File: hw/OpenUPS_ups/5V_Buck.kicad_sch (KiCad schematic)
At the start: 44 parts, among them U301 TPS51397A

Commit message: More cleanups and stuff
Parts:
- removed C?: 100n 50V, Capacitor_SMD:C_0603_1608Metric, symbol Device:C_Small
- removed C? (x2): 865080243008, Capacitor_SMD:CP_Elec_6.3x5.7, symbol Device:C_Polarized
- removed C?: 1u, Capacitor_SMD:C_0603_1608Metric, symbol Device:C_Small
- removed C?: 56p, Capacitor_SMD:C_0603_1608Metric, symbol Device:C_Small
- removed C?: 10u 35V, Capacitor_SMD:C_1206_3216Metric, symbol Device:C
- removed C? (x2): 47u 35V, Capacitor_SMD:CP_Elec_6.3x7.7, symbol Device:C_Polarized
- removed C?: ?, Capacitor_SMD:C_0603_1608Metric, symbol Device:C_Small
- removed C?: 1u 35V, Capacitor_SMD:C_1206_3216Metric, symbol Device:C
- removed C?: 12n, Capacitor_SMD:C_0603_1608Metric, symbol Device:C_Small
- removed L?: SRP1038C-3R3M, Inductor_SMD:L_Bourns_SRP1038C_10.0x10.0mm, symbol Device:L
- removed Q? (x2): Q_NMOS_GDS, Package_TO_SOT_SMD:TO-263-2, symbol Device:Q_NMOS_GDS
- removed R?: 4k7, Resistor_SMD:R_0603_1608Metric, symbol Device:R_Small
- removed R? (x4): ?, Resistor_SMD:R_0603_1608Metric, symbol Device:R_Small
- removed R?: 100k, Resistor_SMD:R_0603_1608Metric, symbol Device:R_Small
- removed R?: 0R, Resistor_SMD:R_0603_1608Metric, symbol Device:R_Small
- removed R?: 1k, Resistor_SMD:R_0603_1608Metric, symbol Device:R_Small
- removed U?: NCP3011, Package_SO:TSSOP-16_4.4x5mm_P0.65mm, symbol open-psu:NCP3011
- gave numbers to parts that had none: 2
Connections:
- net EN: now reaches R306.1, R307.2, U301.12 (EN)
- no-connect marks 2 -> 0
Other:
- note removed: "ISen"
- moved on the sheet: C301, C302, C303, C304, C305, C306, C307, C308, C309, C310, L301, R301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

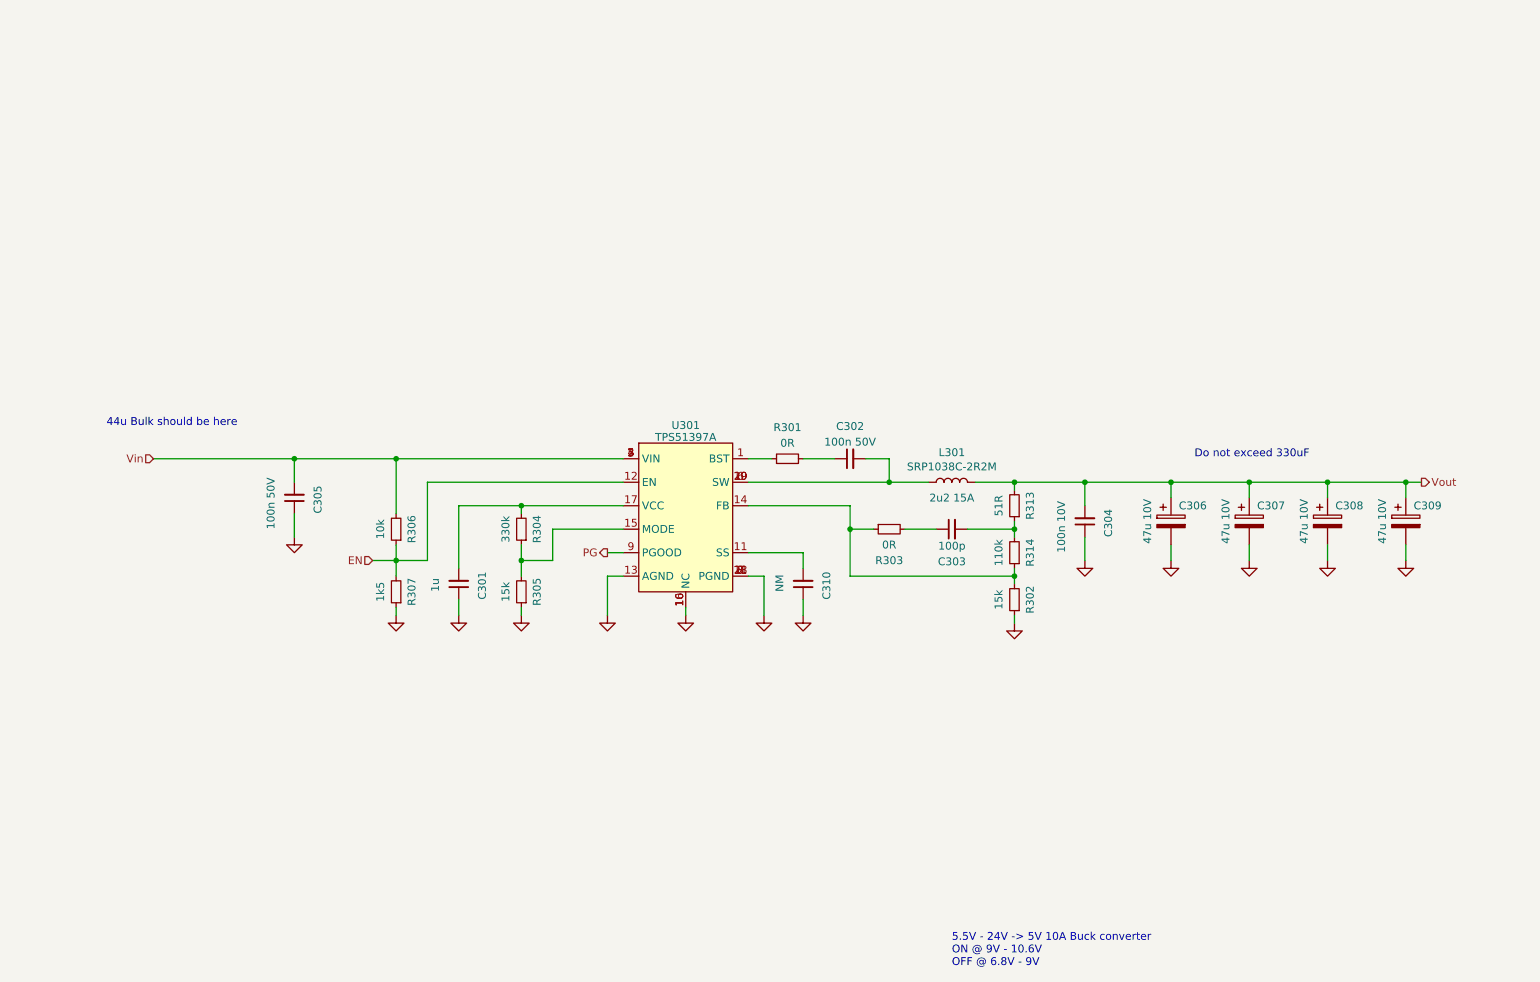
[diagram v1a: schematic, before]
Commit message: Work on 5V; EN pins taken care of.
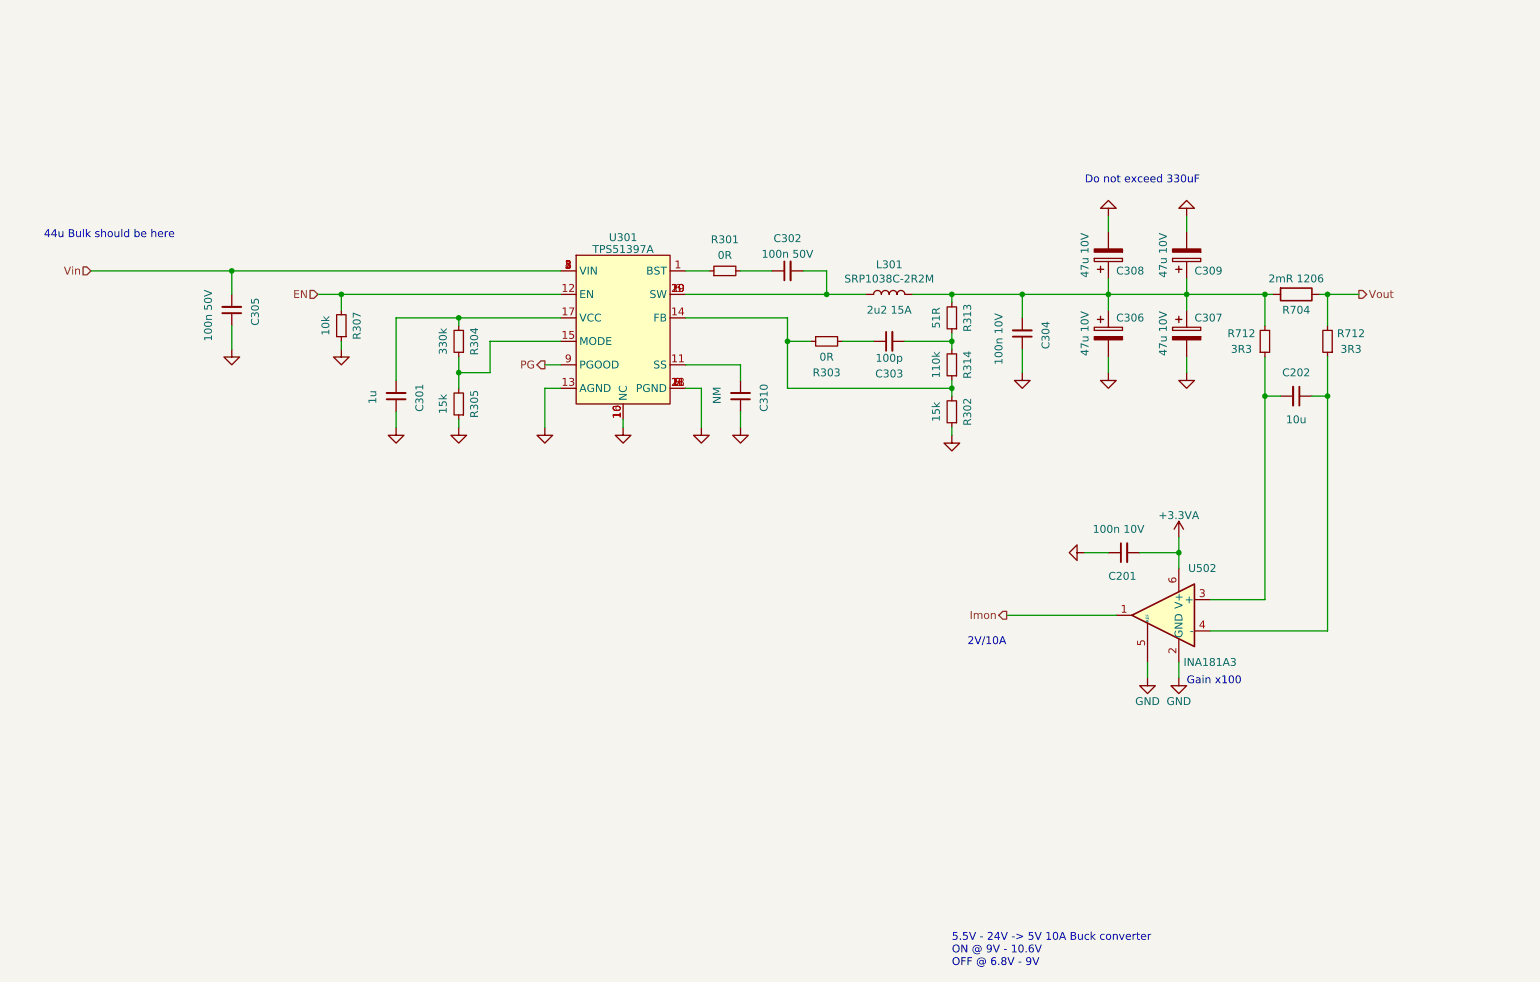
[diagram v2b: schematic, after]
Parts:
- removed R306: 10k, Resistor_SMD:R_0603_1608Metric, symbol Device:R_Small
- added C201: 100n 10V, Capacitor_SMD:C_0603_1608Metric, symbol Device:C_Small
- added C202: 10u, Capacitor_SMD:C_0603_1608Metric, symbol Device:C_Small
- added R704: 2mR 1206, Resistor_SMD:R_1206_3216Metric, symbol Device:R
- added R712 (x2): 3R3, Resistor_SMD:R_0603_1608Metric, symbol Device:R_Small
- added U502: INA181A3, Package_TO_SOT_SMD:SOT-23-6, symbol Amplifier_Current:INA181
- R307: value 1k5 -> 10k
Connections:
- net GND: now also C201.1, U502.2 (GND), U502.5 (REF)
- net Vout: now also R704.1, R712.2; no longer C304.2, C306.1, C307.1, C308.1, C309.1, L301.2, R313.2
- new net: C304.2, C306.1, C307.1, C308.1, C309.1, L301.2, R313.2, R704.2, R712.2
- new net: C202.1, R712.1, U502.4 (-)
- new net: C202.2, R712.1, U502.3 (+)
- new net +3.3VA: C201.2, U502.6 (V+)
- new net Imon: U502.1
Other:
- note added: "2V/10A"
- note added: "Gain x100"
- moved on the sheet: C301, C302, C303, C304, C305, C306, C307, C308, C309, C310, L301, R301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

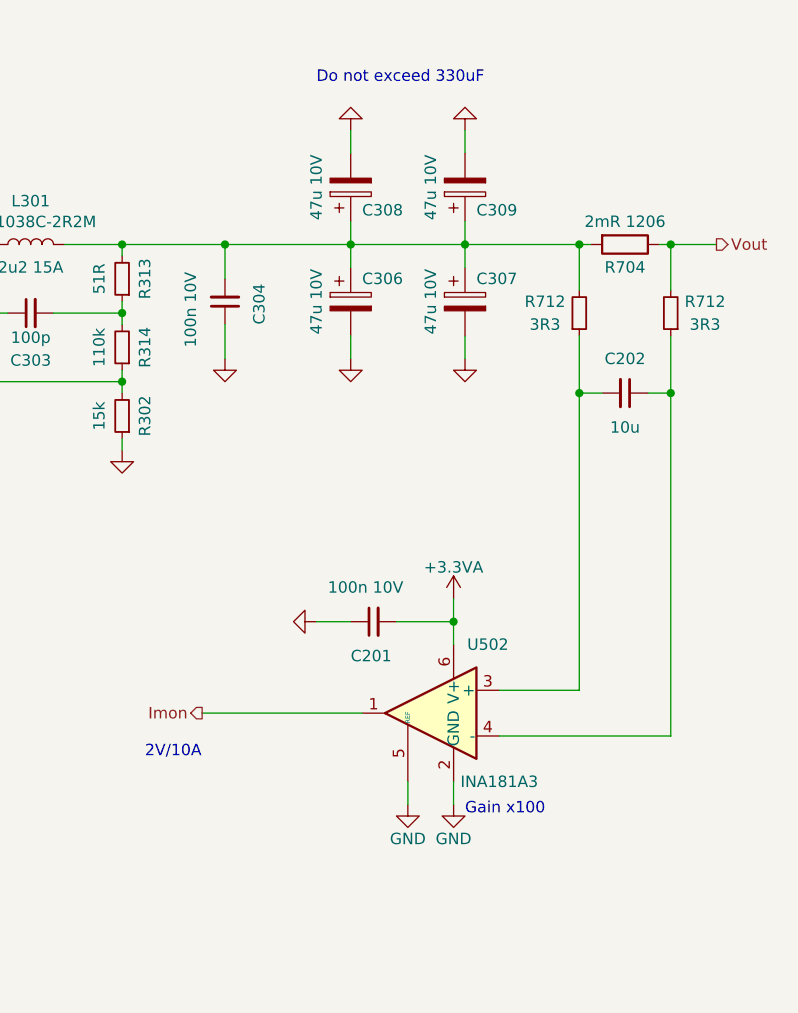
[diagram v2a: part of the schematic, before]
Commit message: Preliminary NMOS: AON7534; USB-C selected.
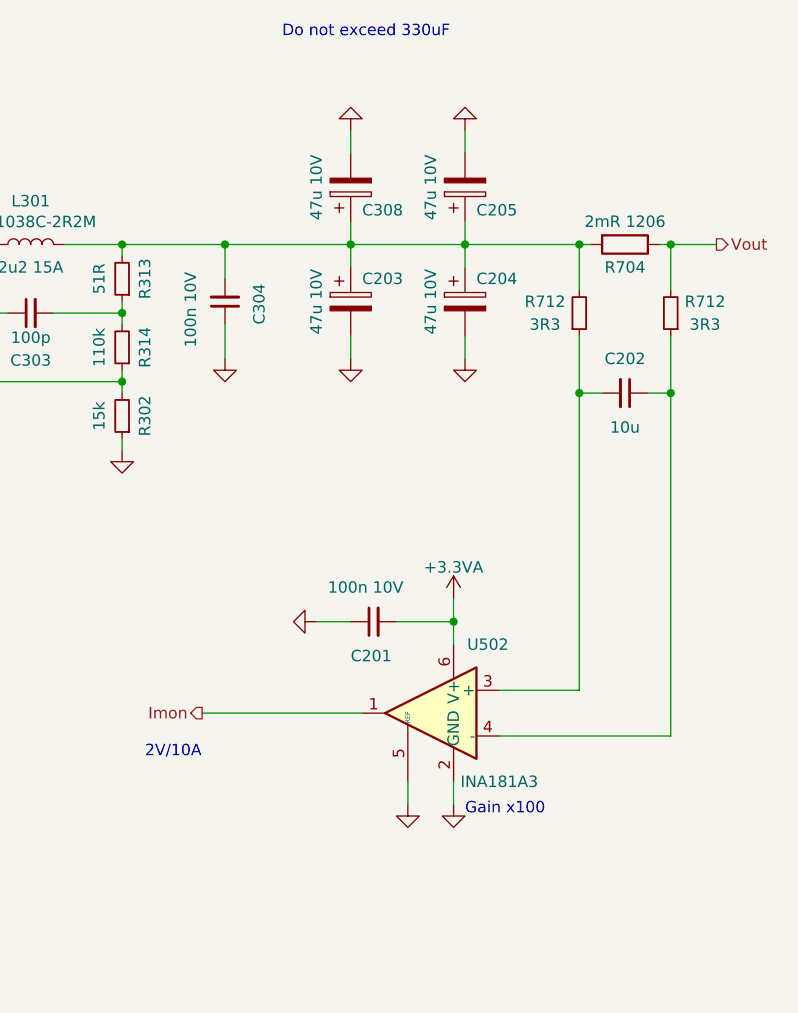
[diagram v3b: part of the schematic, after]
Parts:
- removed C306, C307, C309: ~, Capacitor_SMD:CP_Elec_6.3x5.7, symbol Device:C_Polarized
- added C203, C204, C205: 16ZLG47MEFC6.3X7, Capacitor_THT:CP_Radial_D6.3mm_P2.50mm, symbol Device:C_Polarized
- C308: value ~ -> 16ZLG47MEFC6.3X7; footprint Capacitor_SMD:CP_Elec_6.3x5.7 -> Capacitor_THT:CP_Radial_D6.3mm_P2.50mm
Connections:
- net GND: now also C203.2, C204.2, C205.2
- net at C304.2, C308.1, L301.2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: now also C203.1, C204.1, C205.1

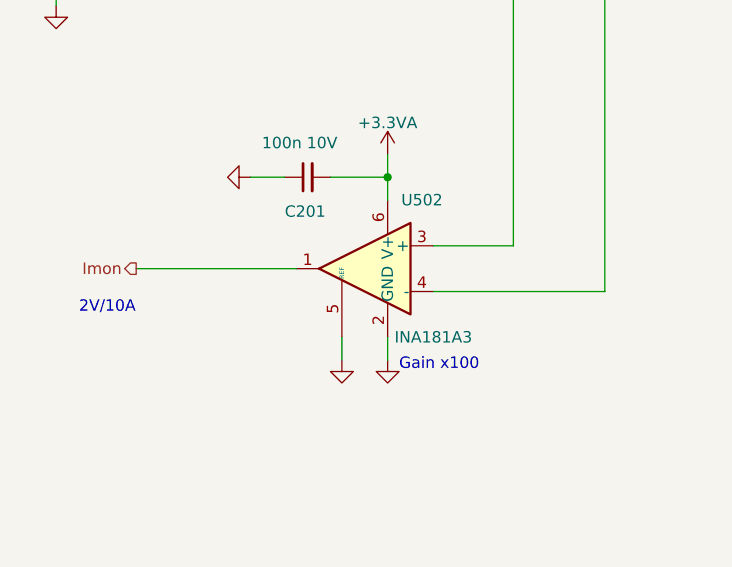
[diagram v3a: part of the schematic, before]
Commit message: Removed Vref (AVR has its own). Replaced INA181s with INA180s
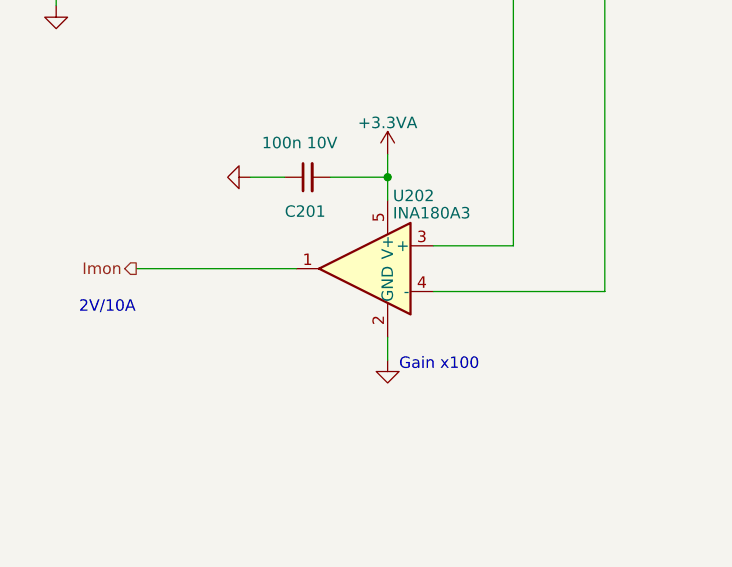
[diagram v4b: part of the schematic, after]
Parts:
- removed U502: INA181A3, Package_TO_SOT_SMD:SOT-23-6, symbol Amplifier_Current:INA181
- added U202: INA180A3, Package_TO_SOT_SMD:SOT-23-5, symbol Amplifier_Current:INA180A3
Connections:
- net +3.3VA: now also U202.5 (V+)
- net GND: now also U202.2 (GND)
- net Imon: now also U202.1
- net at C202.1, R712.1: now also U202.4 (-)
- net at C202.2, R712.1: now also U202.3 (+)

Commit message: Initial placement effort
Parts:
- renumbered C305 to C201, C301 to C202, C310 to C203, C302 to C204, C303 to C205, C304 to C206, C308 to C207, C203 to C208, C201 to C209, C205 to C210, C204 to C211, C202 to C212, L301 to L201, R307 to R201, R304 to R202, R305 to R203, R301 to R204, R303 to R205, R313 to R206, R314 to R207, R302 to R208, U301 to U201

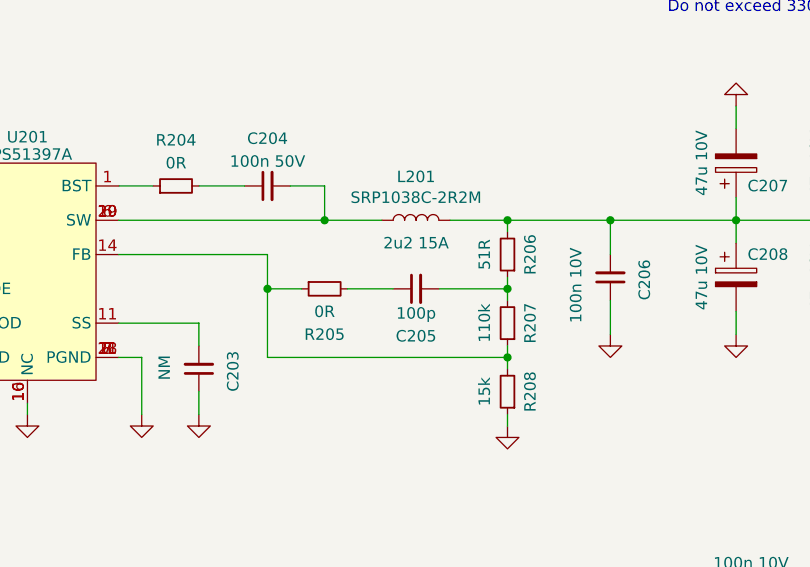
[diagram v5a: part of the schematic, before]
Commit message: Layout: Component models, mechanical, connectors
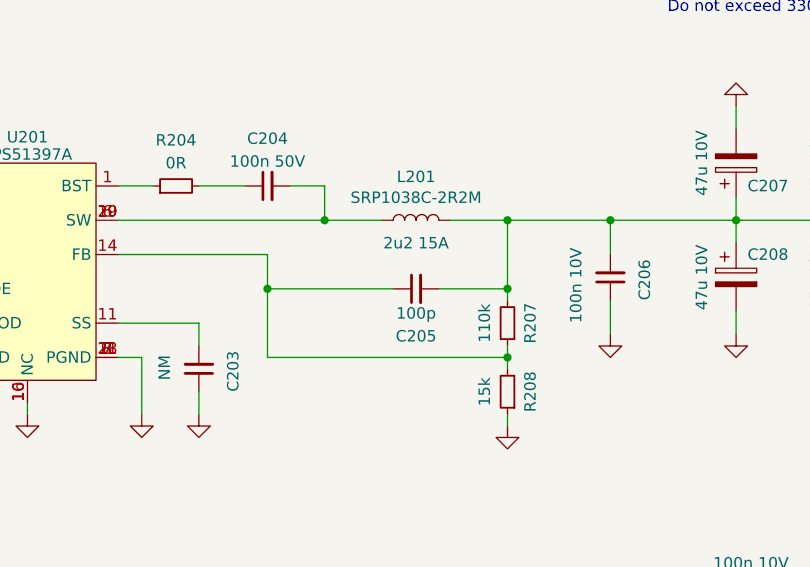
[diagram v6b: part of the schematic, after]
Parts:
- removed R205: 0R, Resistor_SMD:R_0603_1608Metric, symbol Device:R_Small
- removed R206: 51R, Resistor_SMD:R_0603_1608Metric, symbol Device:R_Small
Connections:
- net at R207.1, R208.2, U201.14 (FB): now also C205.1
- net at C206.2, C207.1, C208.1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: now also C205.2, R207.2
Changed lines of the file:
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@@
     (stroke (width 0) (type default))
   )
-  (wire (pts (xy 161.29 73.66) (xy 166.37 73.66))
+  (wire (pts (xy 152.4 73.66) (xy 166.37 73.66))
     (stroke (width 0) (type default))
   )
@@
     (stroke (width 0) (type default))
   )
-  (wire (pts (xy 156.21 73.66) (xy 152.4 73.66))
-    (stroke (width 0) (type default))
-  )
   (wire (pts (xy 179.07 81.28) (xy 152.4 81.28))
     (stroke (width 0) (type default))
@@
     (stroke (width 0) (type default))
   )
-  (wire (pts (xy 179.07 72.39) (xy 179.07 73.66))
-    (stroke (width 0) (type default))
-  )
   (wire (pts (xy 158.75 66.04) (xy 158.75 62.23))
     (stroke (width 0) (type default))
@@
     (stroke (width 0) (type default))
   )
-  (wire (pts (xy 179.07 67.31) (xy 179.07 66.04))
+  (wire (pts (xy 179.07 66.04) (xy 179.07 73.66))
     (stroke (width 0) (type default))
   )
@@
         (path "/f77faec3-eac4-47f3-a2de-ec4a039f4502/c1f639ea-b62e-4979-b175-523e44c4a4ee"
           (reference "L201") (unit 1)
-        )
-      )
-    )
-  )
-  (symbol (lib_id "Device:R_Small") (at 179.07 69.85 180) (unit 1)
-    (in_bom yes) (on_board yes) (dnp no)
-    (property "Reference" "R206" (at 181.61 69.85 90)
-      (effects (font (size 1.27 1.27)))
-    )
-    (property "Value" "51R" (at 176.53 69.85 90)
-      (effects (font (size 1.27 1.27)))
-    )
-    (property "Footprint" "Resistor_SMD:R_0603_1608Metric" (at 179.07 69.85 0)
-      (effects (font (size 1.27 1.27)) hide)
-    )
-    (property "Datasheet" "~" (at 179.07 69.85 0)
-      (effects (font (size 1.27 1.27)) hide)
-    )
-    (pin "1")
-    (pin "2")
-    (instances
-      (project "OpenUPS_ups"
-        (path "/f77faec3-eac4-47f3-a2de-ec4a039f4502/c1f639ea-b62e-4979-b175-523e44c4a4ee"
-          (reference "R206") (unit 1)
         )
       )
@@
         )
       )
-    )
-  )
-  (symbol (lib_id "Device:R_Small") (at 158.75 73.66 90) (mirror x) (unit 1)
-    (in_bom yes) (on_board yes) (dnp no)
-    (property "Reference" "R205" (at 158.75 78.74 90)
-      (effects (font (size 1.27 1.27)))
-    )
-    (property "Value" "0R" (at 158.75 76.2 90)
-      (effects (font (size 1.27 1.27)))
-    )
-    (property "Footprint" "Resistor_SMD:R_0603_1608Metric" (at 158.75 73.66 0)
-      (effects (font (size 1.27 1.27)) hide)
-    )
-    (property "Datasheet" "~" (at 158.75 73.66 0)
-      (effects (font (size 1.27 1.27)) hide)
-    )
-    (pin "1")
-    (pin "2")
-    (instances
-      (project "OpenUPS_ups"
-        (path "/f77faec3-eac4-47f3-a2de-ec4a039f4502/c1f639ea-b62e-4979-b175-523e44c4a4ee"
-          (reference "R205") (unit 1)
-        )
-      )

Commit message: PCB placement
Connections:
- net Vout: now also C207.1, C208.1, C210.1, C211.1
- net at C205.2, C206.2, L201.2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: no longer C207.1, C208.1, C210.1, C211.1
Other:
- moved on the sheet: C201, C202, C203, C204, C205, C206, C207, C208, C209, C210, C211, C212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
